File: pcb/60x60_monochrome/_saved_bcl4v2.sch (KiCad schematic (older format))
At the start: 29 parts, among them Q1 BSS138, SW1 SW_Push, SW2 SW_Push, SW3 SW_Push, U1 DS9166A-23, U2 STM32F070CBTx, Y1 Resonator

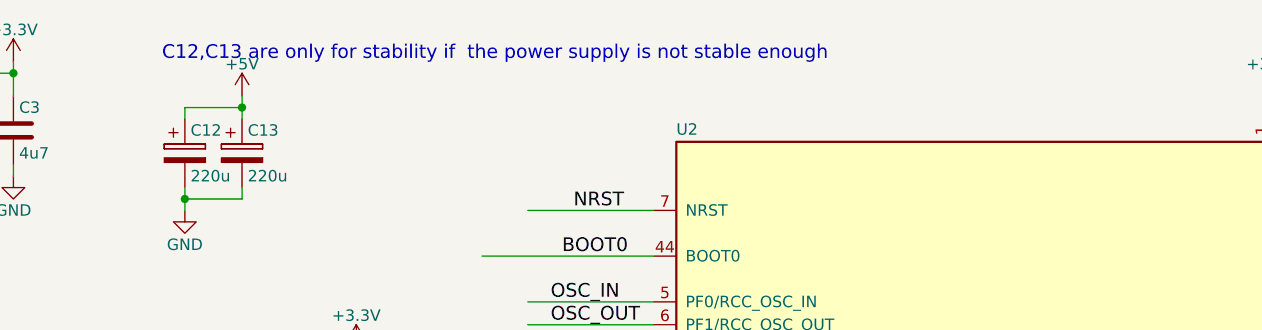
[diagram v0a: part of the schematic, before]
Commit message: - replaced protection LEDs with mosfet
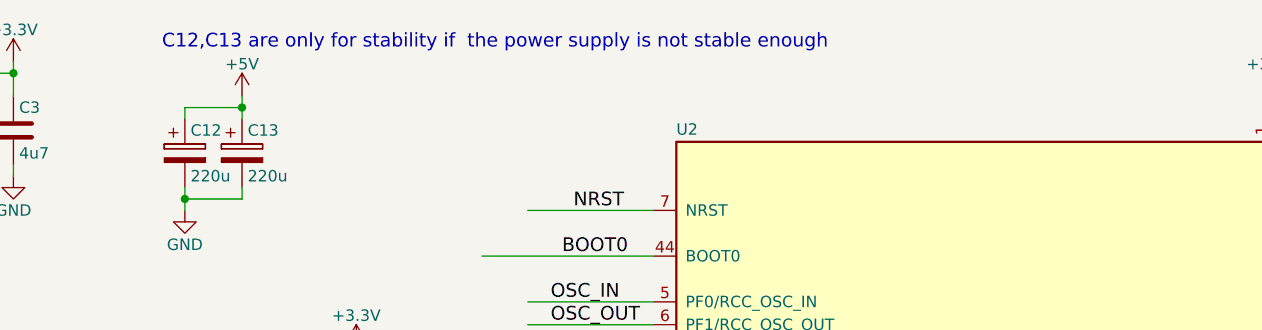
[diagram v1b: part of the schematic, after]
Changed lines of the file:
@@
 Shottky level shifter,\ntogether with the internal pull-up.\nR to GND is for analog in possibility\nin that case replace the D with resistor\nto create a voltage divider\n
 $Comp
-L +3.3V #PWR03
+L +3.3V #PWR02
 U 1 1 5B7CDF17
 P 1800 900
-F 0 "#PWR03" H 1800 750 50  0001 C CNN
+F 0 "#PWR02" H 1800 750 50  0001 C CNN
 F 1 "+3.3V" H 1800 1040 50  0000 C CNN
 F 2 "" H 1800 900 50  0001 C CNN
@@
 $EndComp
 $Comp
-L +3.3V #PWR04
+L +3.3V #PWR03
 U 1 1 5B7CDF67
 P 1100 3250
-F 0 "#PWR04" H 1100 3100 50  0001 C CNN
+F 0 "#PWR03" H 1100 3100 50  0001 C CNN
 F 1 "+3.3V" H 1100 3390 50  0000 C CNN
 F 2 "" H 1100 3250 50  0001 C CNN
@@
 $EndComp
 $Comp
-L +3.3V #PWR05
+L +3.3V #PWR04
 U 1 1 5B7CDFA3
 P 7300 1050
-F 0 "#PWR05" H 7300 900 50  0001 C CNN
+F 0 "#PWR04" H 7300 900 50  0001 C CNN
 F 1 "+3.3V" H 7300 1190 50  0000 C CNN
 F 2 "" H 7300 1050 50  0001 C CNN
@@
 $EndComp
 $Comp
-L +3.3V #PWR07
+L +3.3V #PWR05
 U 1 1 5B8967C1
 P 1950 3150
-F 0 "#PWR07" H 1950 3000 50  0001 C CNN
+F 0 "#PWR05" H 1950 3000 50  0001 C CNN
 F 1 "+3.3V" H 1950 3290 50  0000 C CNN
 F 2 "" H 1950 3150 50  0001 C CNN
@@
 $EndComp
 $Comp
-L +3.3V #PWR08
+L +3.3V #PWR06
 U 1 1 5BD4A8F0
 P 2650 3150
-F 0 "#PWR08" H 2650 3000 50  0001 C CNN
+F 0 "#PWR06" H 2650 3000 50  0001 C CNN
 F 1 "+3.3V" H 2650 3290 50  0000 C CNN
 F 2 "" H 2650 3150 50  0001 C CNN
@@
 BTN1
 $Comp
-L GND #PWR09
+L GND #PWR07
 U 1 1 5BD581B6
 P 700 1350
-F 0 "#PWR09" H 700 1100 50  0001 C CNN
+F 0 "#PWR07" H 700 1100 50  0001 C CNN
 F 1 "GND" H 700 1200 50  0000 C CNN
 F 2 "" H 700 1350 50  0001 C CNN
@@
 $EndComp
 $Comp
-L GND #PWR010
+L GND #PWR08
 U 1 1 5BD5842F
 P 1150 1350
-F 0 "#PWR010" H 1150 1100 50  0001 C CNN
+F 0 "#PWR08" H 1150 1100 50  0001 C CNN
 F 1 "GND" H 1150 1200 50  0000 C CNN
 F 2 "" H 1150 1350 50  0001 C CNN
@@
 $EndComp
 $Comp
-L GND #PWR011
+L GND #PWR09
 U 1 1 5BD584A7
 P 1800 1400
-F 0 "#PWR011" H 1800 1150 50  0001 C CNN
+F 0 "#PWR09" H 1800 1150 50  0001 C CNN
 F 1 "GND" H 1800 1250 50  0000 C CNN
 F 2 "" H 1800 1400 50  0001 C CNN
@@
 $EndComp
 $Comp
-L GND #PWR012
+L GND #PWR010
 U 1 1 5BD585E9
 P 2650 4100
-F 0 "#PWR012" H 2650 3850 50  0001 C CNN
+F 0 "#PWR010" H 2650 3850 50  0001 C CNN
 F 1 "GND" H 2650 3950 50  0000 C CNN
 F 2 "" H 2650 4100 50  0001 C CNN
@@
 $EndComp
 $Comp
-L GND #PWR013
+L GND #PWR011
 U 1 1 5BD58661
 P 1950 4100
-F 0 "#PWR013" H 1950 3850 50  0001 C CNN
+F 0 "#PWR011" H 1950 3850 50  0001 C CNN
 F 1 "GND" H 1950 3950 50  0000 C CNN
 F 2 "" H 1950 4100 50  0001 C CNN
@@
 $EndComp
 $Comp
-L GND #PWR014
+L GND #PWR012
 U 1 1 5BD58C74
 P 1150 7400
-F 0 "#PWR014" H 1150 7150 50  0001 C CNN
+F 0 "#PWR012" H 1150 7150 50  0001 C CNN
 F 1 "GND" H 1150 7250 50  0000 C CNN
 F 2 "" H 1150 7400 50  0001 C CNN
@@
 $EndComp
 $Comp
-L GND #PWR015
+L GND #PWR013
 U 1 1 5BD58D1F
 P 2500 7400
-F 0 "#PWR015" H 2500 7150 50  0001 C CNN
+F 0 "#PWR013" H 2500 7150 50  0001 C CNN
 F 1 "GND" H 2500 7250 50  0000 C CNN
 F 2 "" H 2500 7400 50  0001 C CNN
@@
 $EndComp
 $Comp
-L GND #PWR016
+L GND #PWR014
 U 1 1 5BD59223
 P 7300 4700
-F 0 "#PWR016" H 7300 4450 50  0001 C CNN
+F 0 "#PWR014" H 7300 4450 50  0001 C CNN
 F 1 "GND" H 7300 4550 50  0000 C CNN
 F 2 "" H 7300 4700 50  0001 C CNN
@@
 $EndComp
 $Comp
-L GND #PWR017
+L GND #PWR015
 U 1 1 5BD9FBAA
 P 2550 2650
-F 0 "#PWR017" H 2550 2400 50  0001 C CNN
+F 0 "#PWR015" H 2550 2400 50  0001 C CNN
 F 1 "GND" H 2550 2500 50  0000 C CNN
 F 2 "" H 2550 2650 50  0001 C CNN
@@
 $EndComp
 $Comp
-L +3.3V #PWR018
+L +3.3V #PWR016
 U 1 1 5BDA051E
 P 3300 2150
-F 0 "#PWR018" H 3300 2000 50  0001 C CNN
+F 0 "#PWR016" H 3300 2000 50  0001 C CNN
 F 1 "+3.3V" H 3300 2290 50  0000 C CNN
 F 2 "" H 3300 2150 50  0001 C CNN
@@
 $EndComp
 $Comp
-L GND #PWR019
+L GND #PWR017
 U 1 1 5BD5CCBD
 P 1400 2700
-F 0 "#PWR019" H 1400 2450 50  0001 C CNN
+F 0 "#PWR017" H 1400 2450 50  0001 C CNN
 F 1 "GND" H 1400 2550 50  0000 C CNN
 F 2 "" H 1400 2700 50  0001 C CNN
@@
 $EndSheet
 $Comp
-L +3.3V #PWR020
+L +3.3V #PWR018
 U 1 1 5BD77D29
 P 1100 5000
-F 0 "#PWR020" H 1100 4850 50  0001 C CNN
+F 0 "#PWR018" H 1100 4850 50  0001 C CNN
 F 1 "+3.3V" H 1100 5140 50  0000 C CNN
 F 2 "" H 1100 5000 50  0001 C CNN
@@
 $EndComp
 $Comp
-L GND #PWR021
+L GND #PWR019
 U 1 1 5BD77F33
 P 2050 5350
-F 0 "#PWR021" H 2050 5100 50  0001 C CNN
+F 0 "#PWR019" H 2050 5100 50  0001 C CNN
 F 1 "GND" H 2050 5200 50  0000 C CNN
 F 2 "" H 2050 5350 50  0001 C CNN
@@
 $EndComp
 $Comp
-L GND #PWR022
+L GND #PWR020
 U 1 1 5BD77FC0
 P 2550 5350
-F 0 "#PWR022" H 2550 5100 50  0001 C CNN
+F 0 "#PWR020" H 2550 5100 50  0001 C CNN
 F 1 "GND" H 2550 5200 50  0000 C CNN
 F 2 "" H 2550 5350 50  0001 C CNN
@@
 $EndComp
 $Comp
-L GND #PWR023
+L GND #PWR021
 U 1 1 5BD78B14
 P 2250 6150
-F 0 "#PWR023" H 2250 5900 50  0001 C CNN
+F 0 "#PWR021" H 2250 5900 50  0001 C CNN
 F 1 "GND" H 2250 6000 50  0000 C CNN
 F 2 "" H 2250 6150 50  0001 C CNN
@@
 $EndComp
 $Comp
-L GND #PWR024
+L GND #PWR022
 U 1 1 5BD78B79
 P 1850 6150
-F 0 "#PWR024" H 1850 5900 50  0001 C CNN
+F 0 "#PWR022" H 1850 5900 50  0001 C CNN
 F 1 "GND" H 1850 6000 50  0000 C CNN
 F 2 "" H 1850 6150 50  0001 C CNN
@@
 $EndComp
 $Comp
-L GND #PWR025
+L GND #PWR023
 U 1 1 5BDA23CE
 P 2550 1550
-F 0 "#PWR025" H 2550 1300 50  0001 C CNN
+F 0 "#PWR023" H 2550 1300 50  0001 C CNN
 F 1 "GND" H 2550 1400 50  0000 C CNN
 F 2 "" H 2550 1550 50  0001 C CNN
@@
 $EndComp
 $Comp
-L +5V #PWR026
+L +5V #PWR024
 U 1 1 5BDA25E1
 P 2800 1050
-F 0 "#PWR026" H 2800 900 50  0001 C CNN
+F 0 "#PWR024" H 2800 900 50  0001 C CNN
 F 1 "+5V" H 2800 1190 50  0000 C CNN
 F 2 "" H 2800 1050 50  0001 C CNN
@@
 	1    0    0    -1
 $EndComp
-Text Notes 2450 900  0    60   ~ 0
+Text Notes 2450 850  0    60   ~ 0
 C12,C13 are only for stability if  the power supply is not stable enough
 Text Label 5400 5050 2    60   ~ 0
